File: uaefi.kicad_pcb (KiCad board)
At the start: 4 copper layers, 135 x 123 mm, 138 parts, among them J1 211PL562L0011, J2 USB_B_Mini, J3 5569-06A2, J6 Conn_01x06, J7 Conn_01x05_Male, J9 USB_C, M1 Module-power_12and5V-0.2, M2 Module-knock-0.2, M3 Module-vr-discrete-0.5, M4 Module-vr-max9924-0.1, M5 Module-wbo-0.5, M6 Module:mega-mcu100/0.3, M7 Module-can-0.1, P1 Pad, P15 Pad, P16 Pad, P17 Pad, P18 Pad, P2 Pad, P3 Pad, P4 Pad, P7 Pad, P8 Pad, Q10 ISL9V3040D3ST, Q11 ISL9V3040D3ST, Q12 ISL9V3040D3ST, Q7 ISL9V3040D3ST, Q8 ISL9V3040D3ST, Q9 ISL9V3040D3ST, U1 TLE9201SG, U10 VNLD5160TR-E, U11 VNLD5160TR-E, U2 TLE9201SG, U3 MPX4/MPXH6400_MAP, U4 MAX31855KASA, U5 JDY-33, U6 VNLD5160TR-E, U7 VNLD5160TR-E, U8 VNLD5160TR-E, U9 VNLD5160TR-E

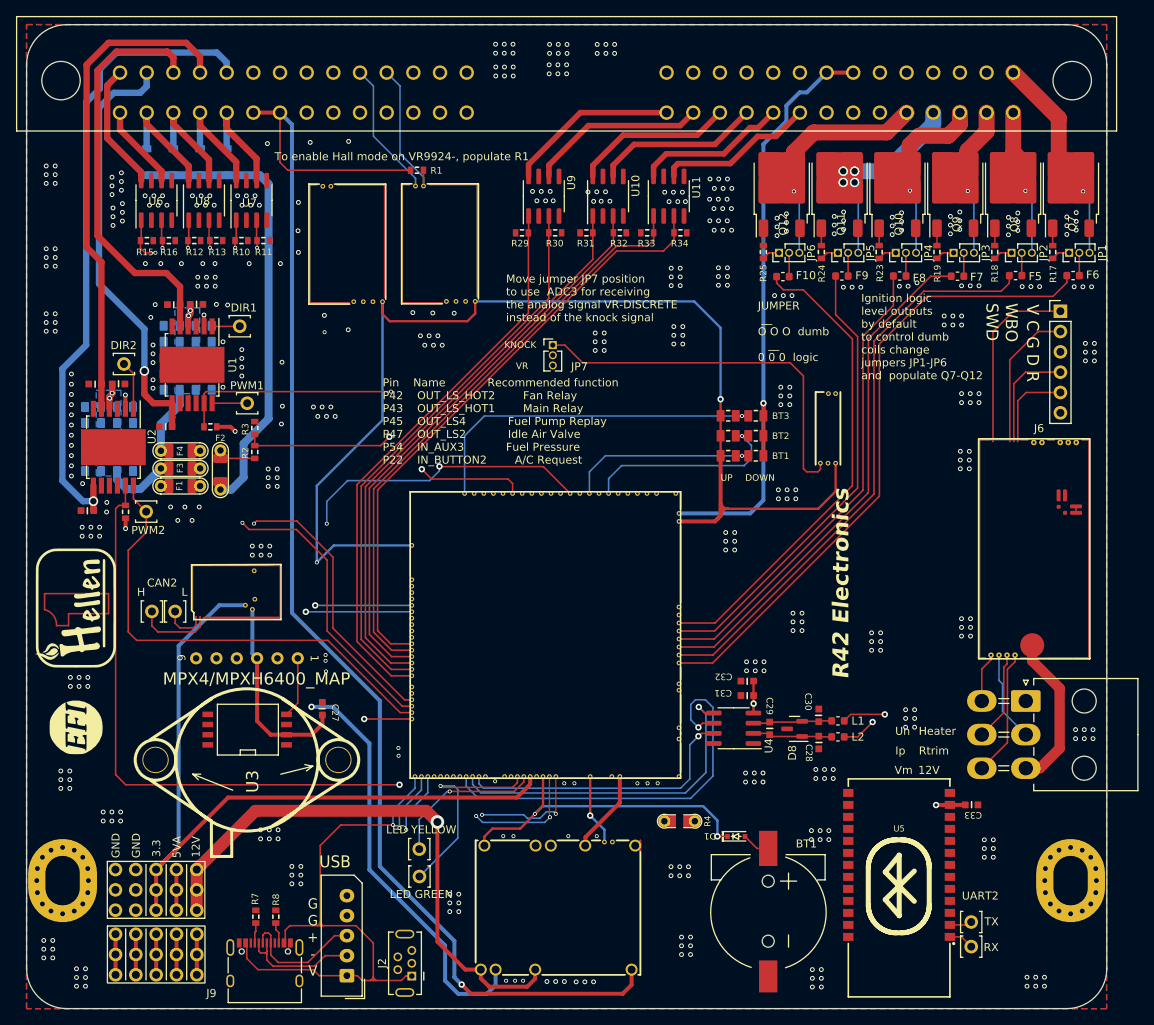
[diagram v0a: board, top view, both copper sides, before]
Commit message: Add Heatsink
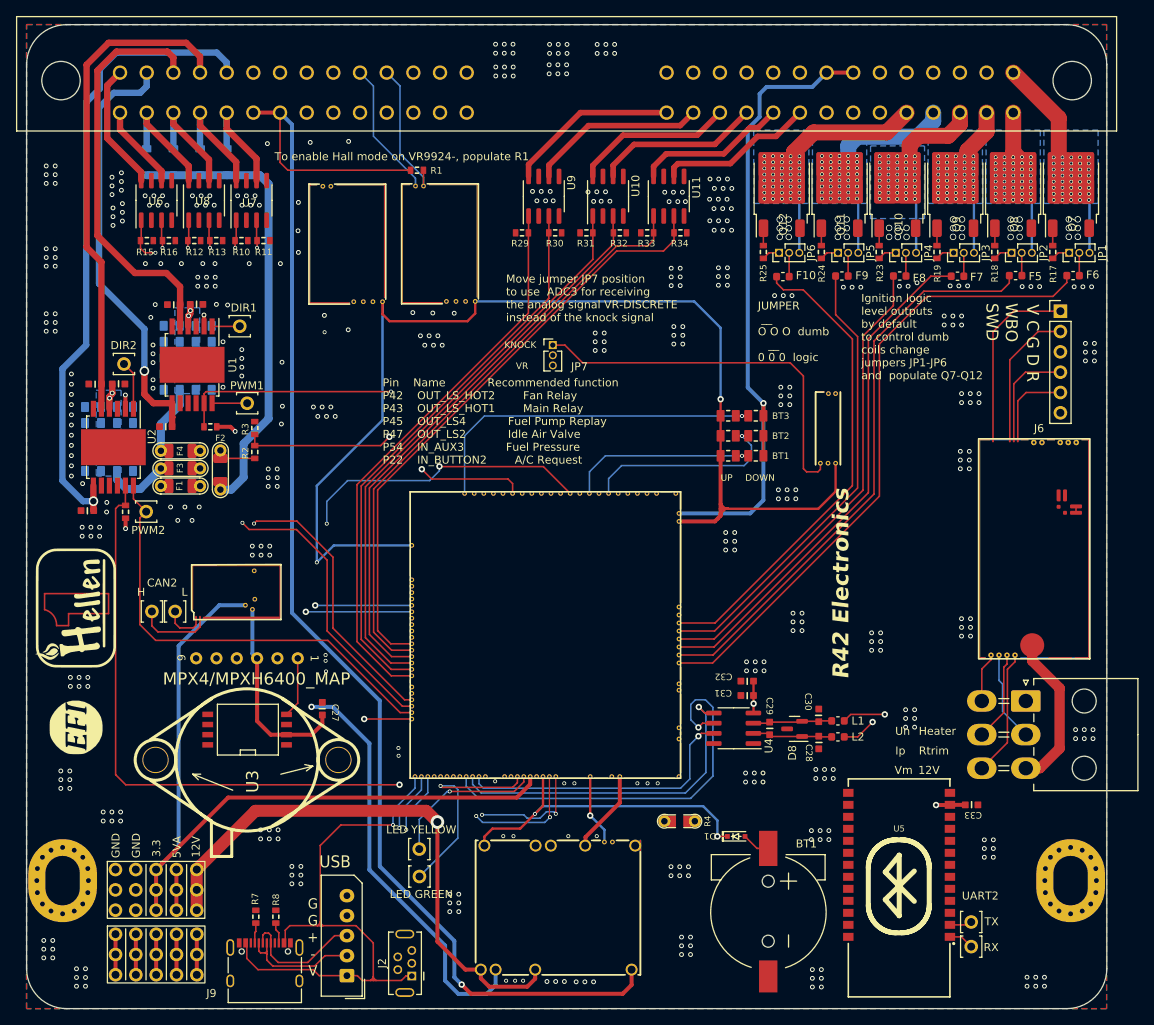
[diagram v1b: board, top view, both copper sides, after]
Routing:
- net GNDA: track 78.4 -> 82.8 mm
- net /DC2_PWM: track 59.5 -> 56.9 mm
- net /OUT_IGN5: track 22.7 -> 21.1 mm, vias 4 -> 40
- net /OUT_IGN2: track 15.2 -> 13.8 mm, vias 1 -> 40
- net /OUT_IGN1: track 21.8 -> 20.5 mm, vias 1 -> 40
- net /CAN+: track 129.9 -> 131.2 mm
- net /OUT_IGN4: track 19.3 -> 18.0 mm, vias 1 -> 40
- net /OUT_IGN3: track 15.5 -> 14.2 mm, vias 1 -> 40
- net /OUT_IGN6: track 25.6 -> 24.4 mm, vias 1 -> 40
- net /EGT+: track 102.3 -> 103.3 mm
- net /EGT-: track 99.4 -> 100.4 mm
- added copper zone on B.Cu, net /OUT_IGN1
- added copper zone on B.Cu, net /OUT_IGN2
- added copper zone on B.Cu, net /OUT_IGN3
- added copper zone on B.Cu, net /OUT_IGN4
- added copper zone on B.Cu, net /OUT_IGN6

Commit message: Add Heatsink
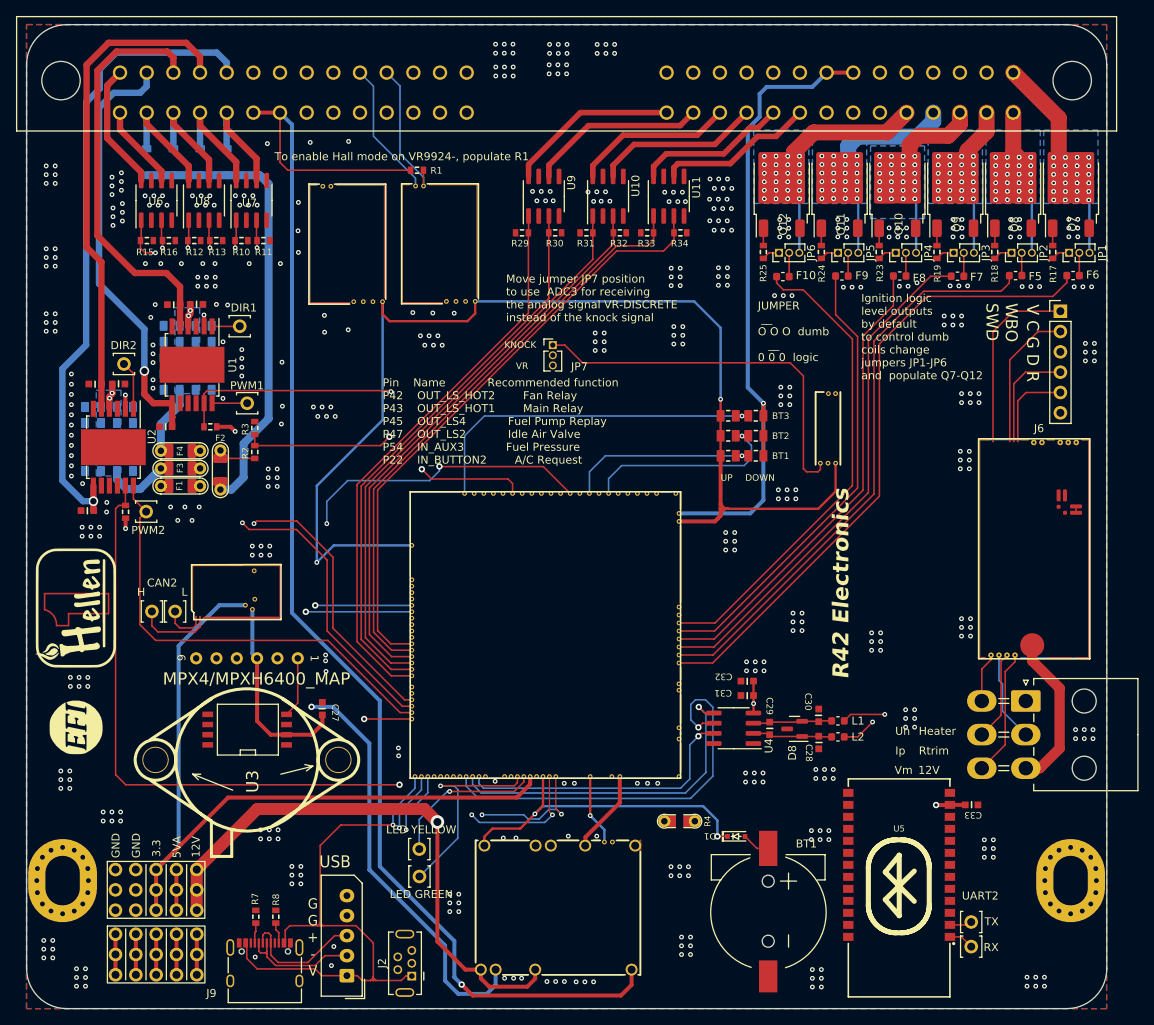
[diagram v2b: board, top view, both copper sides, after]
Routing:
- net /LS_HOT1: track 134.7 -> 121.1 mm
- net /LS_HOT2: track 134.7 -> 122.1 mm
- net /VR_MAX9924: track 93.3 -> 94.7 mm
- net /EGT-: track 100.4 -> 99.1 mm
- net /EGT+: track 103.3 -> 102.1 mm
- net /USB-: track 49.6 -> 48.5 mm
- net /LS3: track 76.1 -> 75.1 mm
- net +12V: track 87.8 -> 88.3 mm
- net GND: vias 481 -> 484
- net /OUT_IGN6: vias 40 -> 24
- net /OUT_IGN5: vias 40 -> 24
- net /OUT_IGN4: vias 40 -> 24
- net /OUT_IGN3: vias 40 -> 24
- net /OUT_IGN2: vias 40 -> 24
- net /OUT_IGN1: vias 40 -> 24
